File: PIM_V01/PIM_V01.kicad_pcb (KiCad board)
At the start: 4 copper layers, 93 x 62 mm, 260 parts, among them J1 Conn_01x06, J10 Conn_02x08_Odd_Even, J11 Conn_01x02, J12 Conn_01x02, J13 Conn_01x02, J4 USB_C_Receptacle_USB2.0_14P, J5 Conn_01x04, J6 Conn_01x04, J7 Conn_02x03_Odd_Even, J8 Conn_01x02, J9 Conn_02x08_Odd_Even, Q1 SQJ407EP-T1_GE3, Q2 PMOS, Q3 PMOS, Q4 NMOS, SW1 SW_Push, U1 TPS259541DSGR, U10 TPS62933, U11 AP2112K-3.3, U12 MP28167GQ-A-P, U13 GD5F1GQ5UEYIGR, U14 MB85RS256B, U2 USBLC6-2SC6, U3 STM32H7A3VITx, U4 MCP2562FDT-E/SN, U5 MCP2562FDT-E/SN, U6 TPS62933, U7 TPS62933, U8 TPS62933, U9 TPS62933, Y1 Crystal_GND24_Small

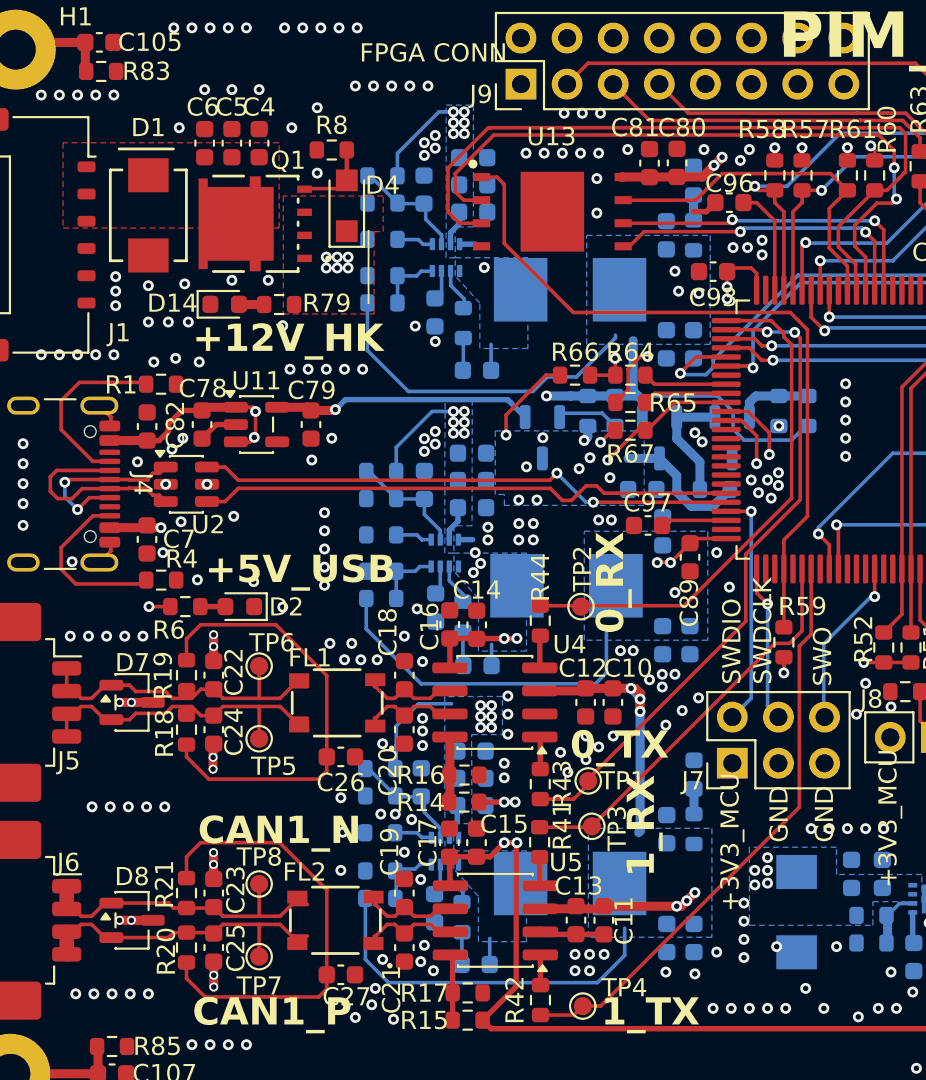
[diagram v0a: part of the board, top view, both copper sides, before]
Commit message: updated the last few component symbols/fps, none very significant
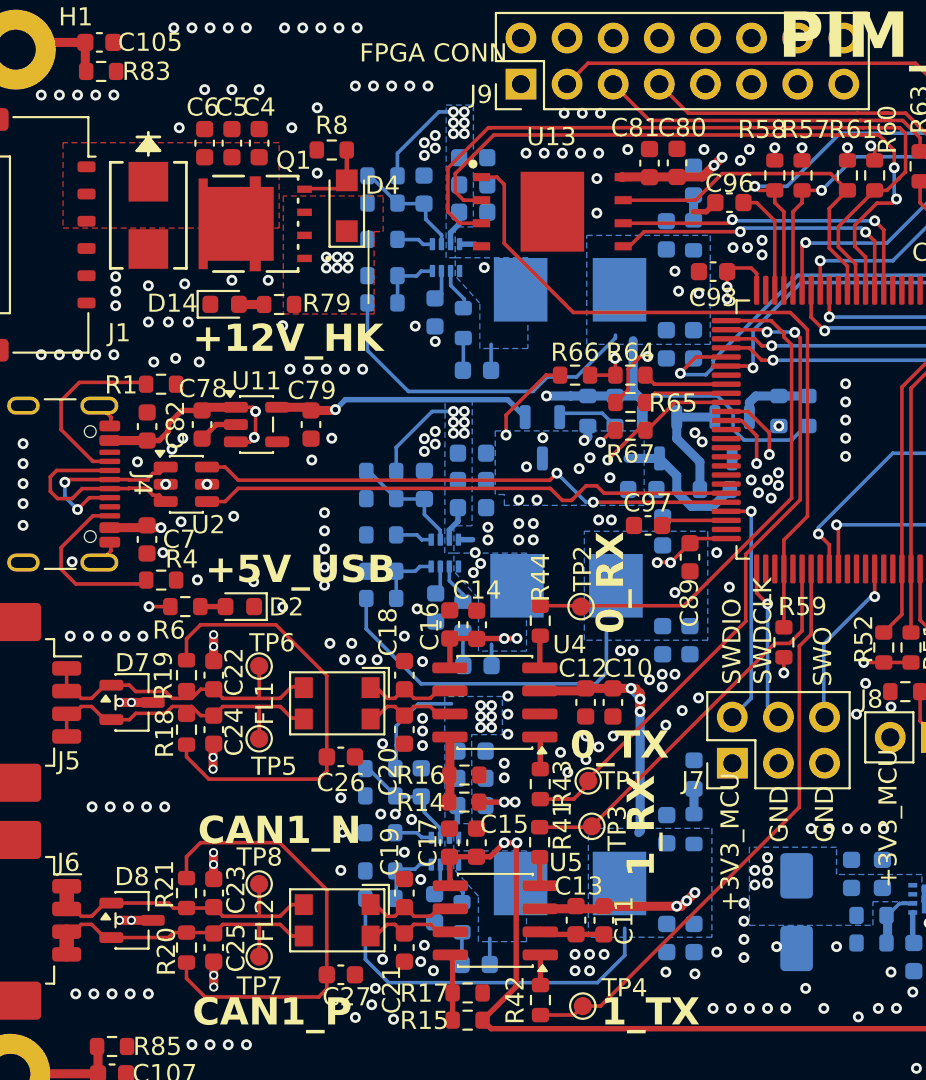
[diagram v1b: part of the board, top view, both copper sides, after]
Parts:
- C1, C104, C72, C78, C79, C8, C80, C95, C99: value C_Small -> 1uF
- C10, C11, C14, C15, C94: value C_Small -> 4.7uF
- C100, C64: value C_Small -> 27pF
- C101, C102, C43, C44, C45, C46, C47, C48, C59, C60, C61, C62, C76, C77: value C_Small -> 22uF
- C103, C12, C13, C16, C17, C2, C34, C35, C36, C40, C41, C42, C53, C54, C57, C58, C70, C73, C74, C81, C83, C84, C85, C86, C87, C88, C89, C90, C91, C92, C93, C98: value C_Small -> 0.1uF
- C105, C106, C107, C108, C38, C55, C56, C65, C66, C67: value C_Small -> 10nF
- C18, C19, C20, C21, C22, C23, C24, C25: value C_Small -> 47pF
- C26, C27: value C_Small -> 4.7nF
- C28, C29, C30, C31, C32, C33, C49, C50, C51, C52, C6, C7, C82, C9: value C_Small -> 10uF
- C3: value C_Small -> 3.3nF
- C37, C39: value C_Small -> 33nF
- C4, C5: value C_Small -> 47uF
- C63: value C_Small -> 100nF
- C68, C75: value C_Small -> 100uF
- C69: value C_Small -> 22uF 25V
- C71: value C_Small -> 22nF
- C96, C97: value C_Small -> 2.2uF
- D1: footprint CustomFootprints:SMBJ12A -> CustomFootprints:SMBJ16A
- D13: footprint CustomFootprints:SMBJ12A -> Diode_SMD:D_SMA
- D3: value D_Schottky -> PMEG4010
- D4: value D_Zener -> BZT52C15
- FL1, FL2: value ACT45B-101-2P-TL003 -> Choke_CommonMode_FerriteCore_1243; footprint CustomFootprints:ACT45B-101-2P-TL003_TDK -> Inductor_SMD:L_CommonModeChoke_Coilcraft_1812CAN
- L1, L2, L3, L4, L5: value L_Small -> 6.8uH
- L6: value L_Small -> 4.7uH
- R1, R4: value R_Small -> 5k1R
- R10, R11, R16, R17, R22, R23, R24, R35, R36, R74, R75, R76, R77, R78, R83, R84, R85, R86, R9: value R_Small -> 0R
- R12, R69: value R_Small -> 1MR
- R13, R14, R15, R26, R28, R30, R38, R40, R59, R60, R61, R66, R67, R7: value R_Small -> 10kR
- R18, R19, R20, R21: value R_Small -> 60R
- R2: value R_Small -> 866kR
- R25, R37: value R_Small -> 52.3kR
- R27, R39: value R_Small -> 31.6kR
- R29: value R_Small -> 4.99kR
- R3: value R_Small -> 150kR
- R31, R33, R6: value R_Small -> 470R
- R32, R34, R81, R82: value R_Small -> 100R
- R41, R42, R43, R44: value R_Small -> 1kR
- R45, R47, R49: value R_Small -> 470kR
- R46, R48, R50, R68, R70, R71, R72, R73, R8: value R_Small -> 100kR
- R5: value R_Small -> 511R
- R51, R52, R57, R58: value R_Small -> 4.7kR
- R53: value R_Small -> 430kR
- R54: value R_Small -> 400kR
- R55: value R_Small -> 21.5kR
- R56: value R_Small -> 43.2kR
- R62, R63, R64, R65: value R_Small -> 33R
- R79, R80: value R_Small -> 1.8kR
- U13: value GD5F1GQ5UEYIGR -> MT29F1G01ABAFDWB-IT_F
- moved FL2 0.10 mm to (107.7, 107.0), turned to -90 degrees
- turned FL1 to -90 degrees
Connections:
- FL1 pad 1: /CAN/CAN0_RAW_P -> /CAN/CAN0_RAW_N
- FL1 pad 2: /CAN/CAN0_RAW_N -> /CAN0_N
- FL1 pad 3: /CAN0_N -> /CAN0_P
- FL1 pad 4: /CAN0_P -> /CAN/CAN0_RAW_P
- FL2 pad 1: /CAN/CAN1_RAW_P -> /CAN/CAN1_RAW_N
- FL2 pad 2: /CAN/CAN1_RAW_N -> /CAN1_N
- FL2 pad 3: /CAN1_N -> /CAN1_P
- FL2 pad 4: /CAN1_P -> /CAN/CAN1_RAW_P
- U13 pad 9: GND -> (no net)
